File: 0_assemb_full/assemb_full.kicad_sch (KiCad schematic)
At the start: 0 parts

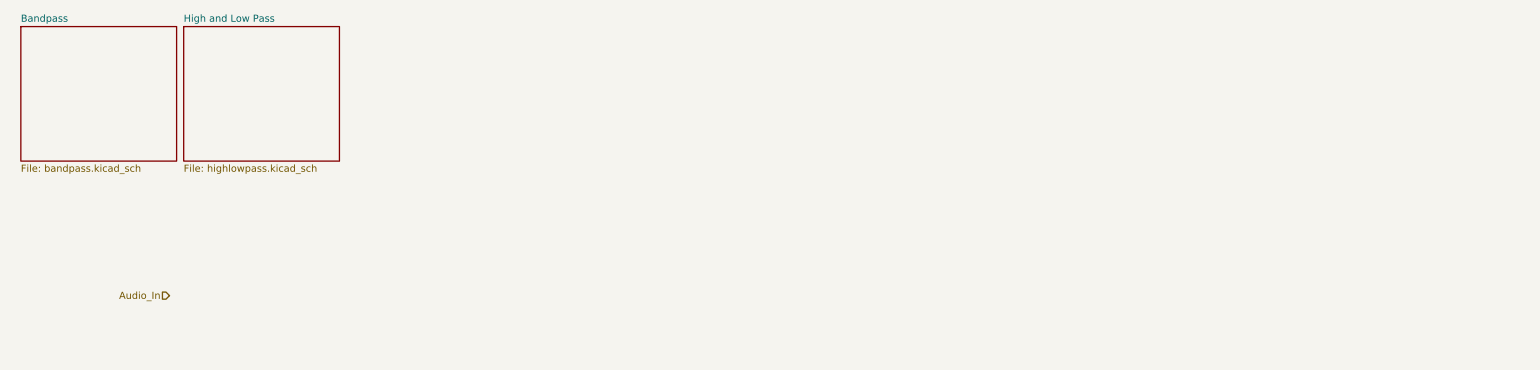
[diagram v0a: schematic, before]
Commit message: Added STM32F091RCTx symbol and power symbols
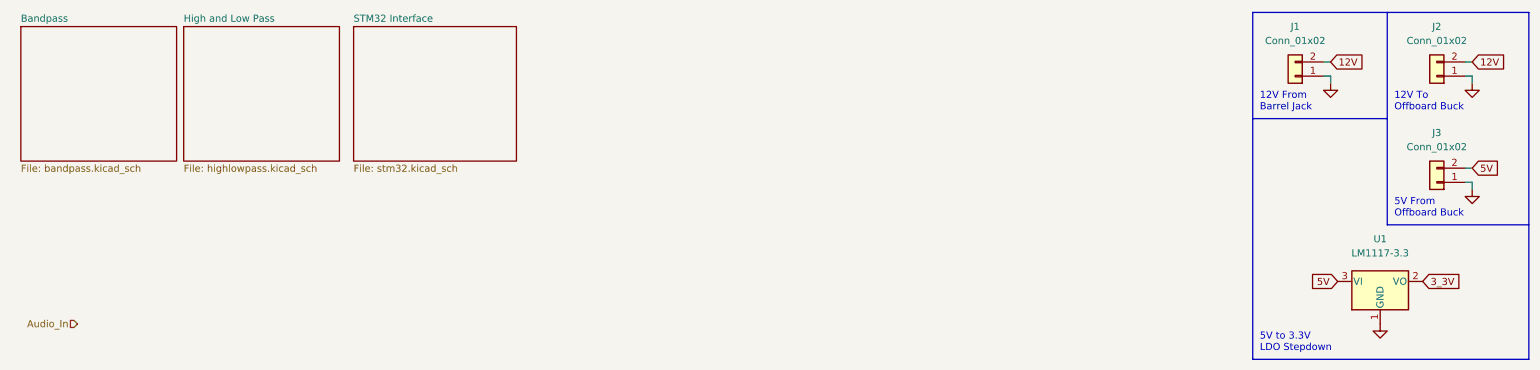
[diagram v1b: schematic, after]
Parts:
- added J1, J2, J3: Conn_01x02, symbol Connector_Generic:Conn_01x02
- added U1: LM1117-3.3, symbol Regulator_Linear:LM1117-3.3
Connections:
- new net 12V: J1.2 (Pin_2), J2.2 (Pin_2)
- new net 3_3V: U1.2 (VO)
- new net 5V: J3.2 (Pin_2), U1.3 (VI)
- new net GND: J1.1 (Pin_1), J2.1 (Pin_1), J3.1 (Pin_1), U1.1 (GND)
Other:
- added sheet STM32 Interface (stm32.kicad_sch)
- note added: "12V From Barrel Jack"
- note added: "12V To Offboard Buck"
- note added: "5V From Offboard Buck"
- note added: "5V to 3.3V LDO Stepdown"

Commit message: Additional changes
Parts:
- added C1, C2: 10u, symbol Device:C
- J1: footprint (none) -> Connector_BarrelJack:BarrelJack_CUI_PJ-102AH_Horizontal
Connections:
- net 12V: now also J1.1 (Pin_1), J2.1 (Pin_1); no longer J1.2 (Pin_2), J2.2 (Pin_2)
- net 3_3V: now also C2.1
- net 5V: now also J3.1 (Pin_1), C1.1; no longer J3.2 (Pin_2)
- net GND: now also J1.2 (Pin_2), J2.2 (Pin_2), J3.2 (Pin_2), C1.2, C2.2; no longer J1.1 (Pin_1), J2.1 (Pin_1), J3.1 (Pin_1)
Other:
- moved on the sheet: J1, J2, J3, U1

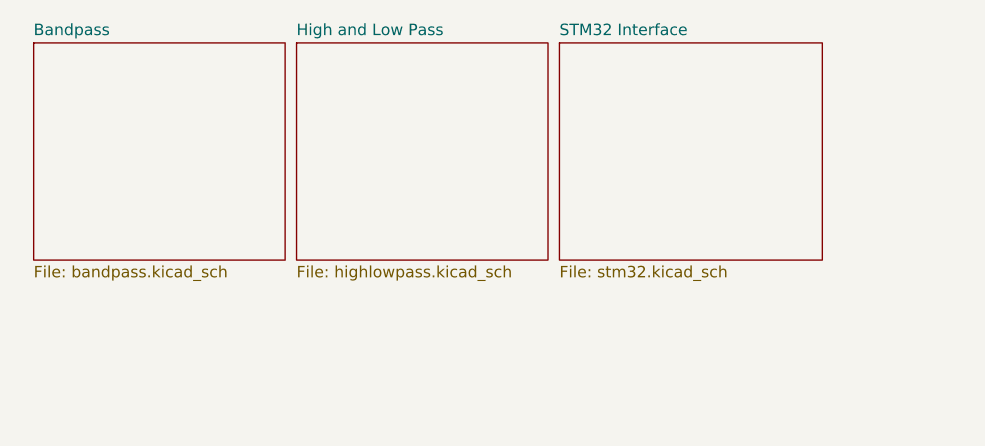
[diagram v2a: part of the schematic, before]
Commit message: Removed varistors, updated some STM32 connections
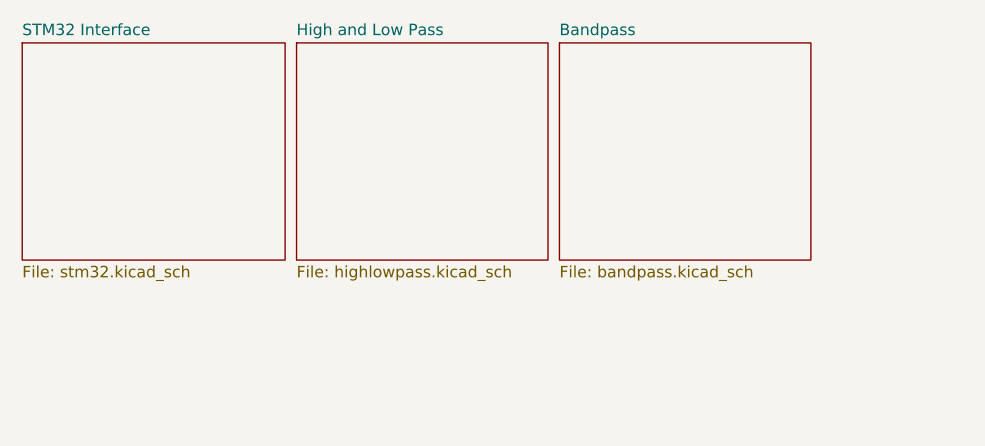
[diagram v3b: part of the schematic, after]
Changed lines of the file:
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@@
     )
   )
-  (sheet (at 13.97 15.24) (size 27.94 24.13) (fields_autoplaced)
+  (sheet (at 72.39 15.24) (size 27.94 24.13) (fields_autoplaced)
     (stroke (width 0.1524) (type solid) (color 0 0 0 0))
     (fill (color 0 0 0 0.0000))
-    (property "Sheet name" "Bandpass" (id 0) (at 13.97 14.5284 0)
+    (property "Sheet name" "Bandpass" (id 0) (at 72.39 14.5284 0)
       (effects (font (size 1.27 1.27)) (justify left bottom))
     )
-    (property "Sheet file" "bandpass.kicad_sch" (id 1) (at 13.97 39.9546 0)
+    (property "Sheet file" "bandpass.kicad_sch" (id 1) (at 72.39 39.9546 0)
       (effects (font (size 1.27 1.27)) (justify left top))
     )
   )
-  (sheet (at 72.39 15.24) (size 29.21 24.13) (fields_autoplaced)
+  (sheet (at 12.7 15.24) (size 29.21 24.13) (fields_autoplaced)
     (stroke (width 0.1524) (type solid) (color 0 0 0 0))
     (fill (color 0 0 0 0.0000))
-    (property "Sheet name" "STM32 Interface" (id 0) (at 72.39 14.5284 0)
+    (property "Sheet name" "STM32 Interface" (id 0) (at 12.7 14.5284 0)
       (effects (font (size 1.27 1.27)) (justify left bottom))
     )
-    (property "Sheet file" "stm32.kicad_sch" (id 1) (at 72.39 39.9546 0)
+    (property "Sheet file" "stm32.kicad_sch" (id 1) (at 12.7 39.9546 0)
       (effects (font (size 1.27 1.27)) (justify left top))
     )
@@
       (reference "J4") (unit 1) (value "Conn_01x02") (footprint "")
     )
+    (path "/4d0bd211-4794-4141-8b4c-fc5ed36fe38a/100fdcba-4ad6-4620-94f4-7ddc5776d3cc"
+      (reference "J5") (unit 1) (value "SPIConn_01x03") (footprint "")
+    )
     (path "/27872fd8-6da5-4d41-bede-b1346c5a5ef3/3c1be632-0e4c-4cdc-9b28-367769451b36"
-      (reference "R1") (unit 1) (value "470") (footprint "")
+      (reference "R1") (unit 1) (value "220") (footprint "")
     )
     (path "/27872fd8-6da5-4d41-bede-b1346c5a5ef3/9db6d9c8-1e04-4846-be6b-7548dbb58116"
-      (reference "R2") (unit 1) (value "470") (footprint "")
+      (reference "R2") (unit 1) (value "220") (footprint "")
     )
     (path "/27872fd8-6da5-4d41-bede-b1346c5a5ef3/83a6c34b-cd42-4bc3-8098-00e2f2514636"
@@
     )
     (path "/27872fd8-6da5-4d41-bede-b1346c5a5ef3/710dc276-e229-4000-a5ad-052650e37413"
-      (reference "R5") (unit 1) (value "470") (footprint "")
+      (reference "R5") (unit 1) (value "220") (footprint "")
     )
     (path "/27872fd8-6da5-4d41-bede-b1346c5a5ef3/05c4cbb0-a462-4ca4-b4c1-4ab919f030b3"
@@
     )
     (path "/016209f3-6b0c-4be6-bf7f-4e52cc050e04/6322e136-6565-4534-9cec-e553b466d6c3"
-      (reference "R26") (unit 1) (value "470") (footprint "")
+      (reference "R26") (unit 1) (value "220") (footprint "")
     )
     (path "/016209f3-6b0c-4be6-bf7f-4e52cc050e04/1fd93811-7681-45f0-be35-117fd0697e16"
-      (reference "R27") (unit 1) (value "4.7K") (footprint "")
+      (reference "R27") (unit 1) (value "680") (footprint "")
     )
     (path "/016209f3-6b0c-4be6-bf7f-4e52cc050e04/1adaa2cb-5868-4644-a777-0e0cd70303f5"
@@
     )
     (path "/016209f3-6b0c-4be6-bf7f-4e52cc050e04/838c7b61-f247-4811-b006-4589bd547892"
-      (reference "R42") (unit 1) (value "470") (footprint "")
+      (reference "R42") (unit 1) (value "220") (footprint "")
     )
     (path "/016209f3-6b0c-4be6-bf7f-4e52cc050e04/e6682f13-8da5-4feb-96ee-693438046242"
@@
     )
     (path "/016209f3-6b0c-4be6-bf7f-4e52cc050e04/8175f77f-1f13-4606-801a-a25d1b77be96"
-      (reference "R45") (unit 1) (value "330") (footprint "")
+      (reference "R45") (unit 1) (value "150") (footprint "")
     )
     (path "/016209f3-6b0c-4be6-bf7f-4e52cc050e04/5ff1d421-f058-4c00-a35d-653f9896f96f"
@@
       (reference "R58") (unit 1) (value "100K") (footprint "")
     )
-    (path "/27872fd8-6da5-4d41-bede-b1346c5a5ef3/86de8196-9bb4-4958-9d15-f4b9c104935b"
-      (reference "RV1") (unit 1) (value "1K") (footprint "")
-    )
-    (path "/27872fd8-6da5-4d41-bede-b1346c5a5ef3/d817147e-f3d1-4948-a7ac-9bc6cf3a8b08"
-      (reference "RV2") (unit 1) (value "1K") (footprint "")
-    )
-    (path "/27872fd8-6da5-4d41-bede-b1346c5a5ef3/1bcd90d8-ea3a-45ad-93f3-8f1c8cea09d3"
-      (reference "RV3") (unit 1) (value "1K") (footprint "")
-    )
-    (path "/016209f3-6b0c-4be6-bf7f-4e52cc050e04/20368424-e0c8-4202-a8a7-d2a77028b7d5"
-      (reference "RV4") (unit 1) (value "1K") (footprint "")
-    )
-    (path "/016209f3-6b0c-4be6-bf7f-4e52cc050e04/b85f2704-e5e8-42e4-b2b2-4e2c7e2225dd"
-      (reference "RV5") (unit 1) (value "10K") (footprint "")
-    )
-    (path "/016209f3-6b0c-4be6-bf7f-4e52cc050e04/ac26d519-1e26-4e03-8b77-68d694fbb77f"
-      (reference "RV6") (unit 1) (value "1K") (footprint "")
-    )
-    (path "/016209f3-6b0c-4be6-bf7f-4e52cc050e04/f9b2ebb7-9757-4a5b-8dcc-2c57fc590e02"
-      (reference "RV7") (unit 1) (value "680") (footprint "")
-    )
     (path "/d3e0143d-69a2-4508-8939-8f6315ecceac"

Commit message: A bunch of changes to the schematics
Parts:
- removed J2, J3: Conn_01x02, symbol Connector_Generic:Conn_01x02
- added J?: Conn_02x06, symbol Connector_Generic:Conn_02x06_Counter_Clockwise
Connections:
- net 12V: now also J?.4 (Pin_4), J?.9 (Pin_9)
- net 5V: now also J?.1 (Pin_1), J?.12 (Pin_12)
- net GND: now also J?.10 (Pin_10), J?.11 (Pin_11), J?.2 (Pin_2), J?.3 (Pin_3)
- new net 12VRP: J?.5 (Pin_5), J?.8 (Pin_8)
- new net ENB: J?.6 (Pin_6)
- new net PGB: J?.7 (Pin_7)
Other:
- note added: "Buck Connections"
- note added: "Copy from STM32 Dev Board?"
- note removed: "12V To Offboard Buck"
- note removed: "5V From Offboard Buck"
- moved on the sheet: C1, C2, U1

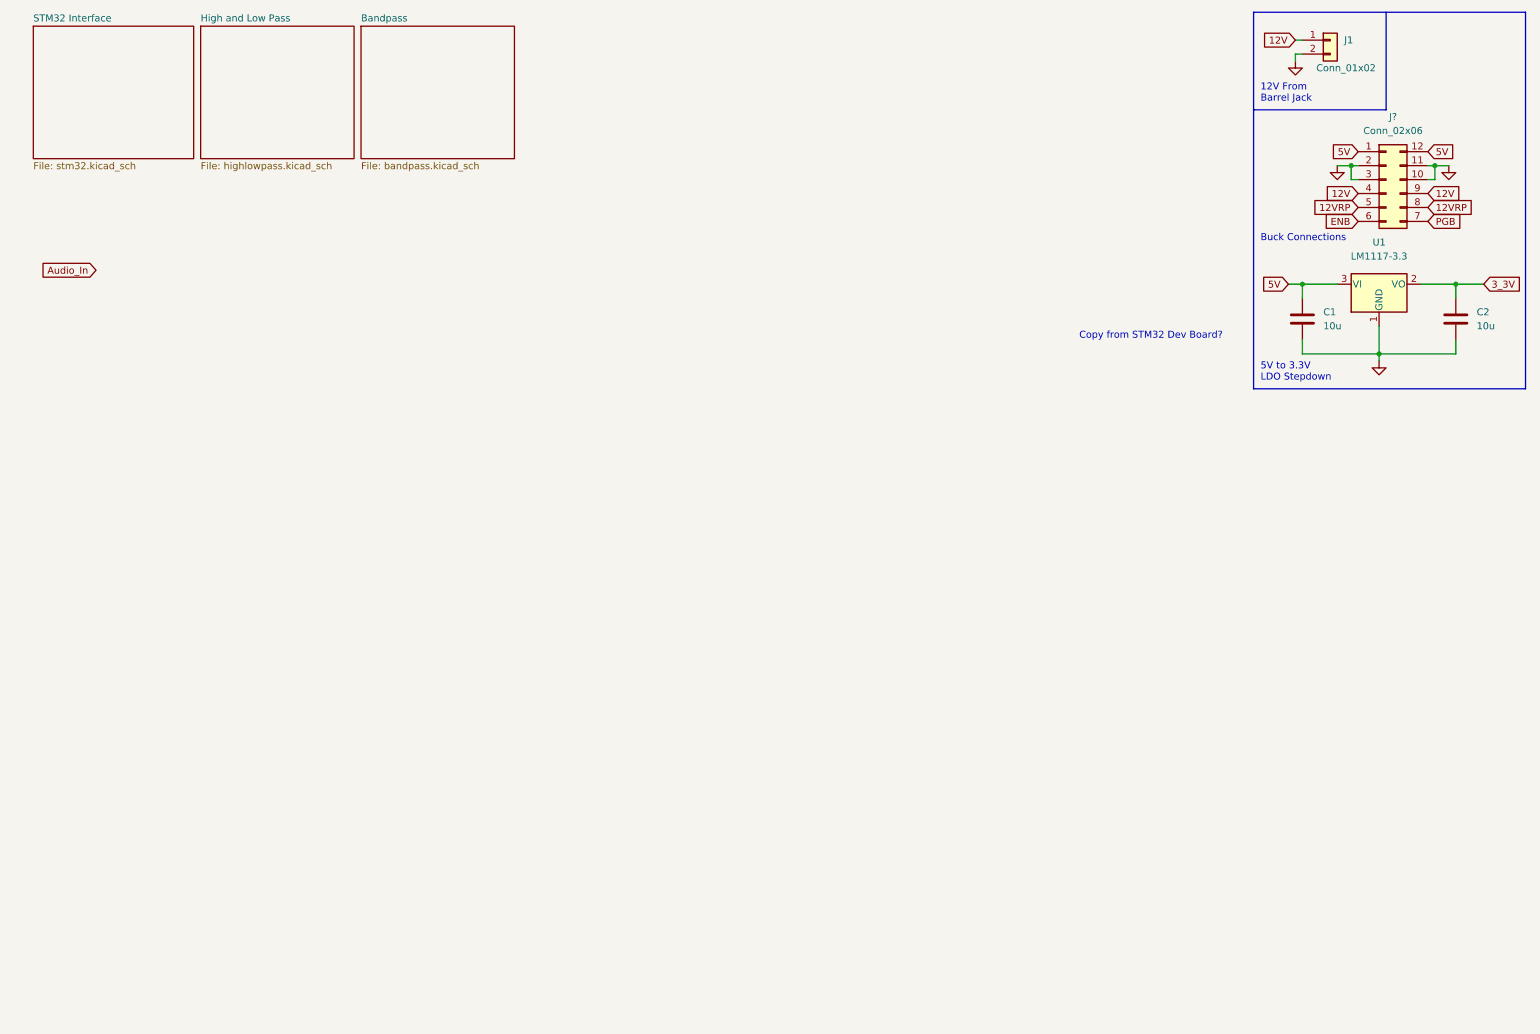
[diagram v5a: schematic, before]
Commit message: Updates to the filter system
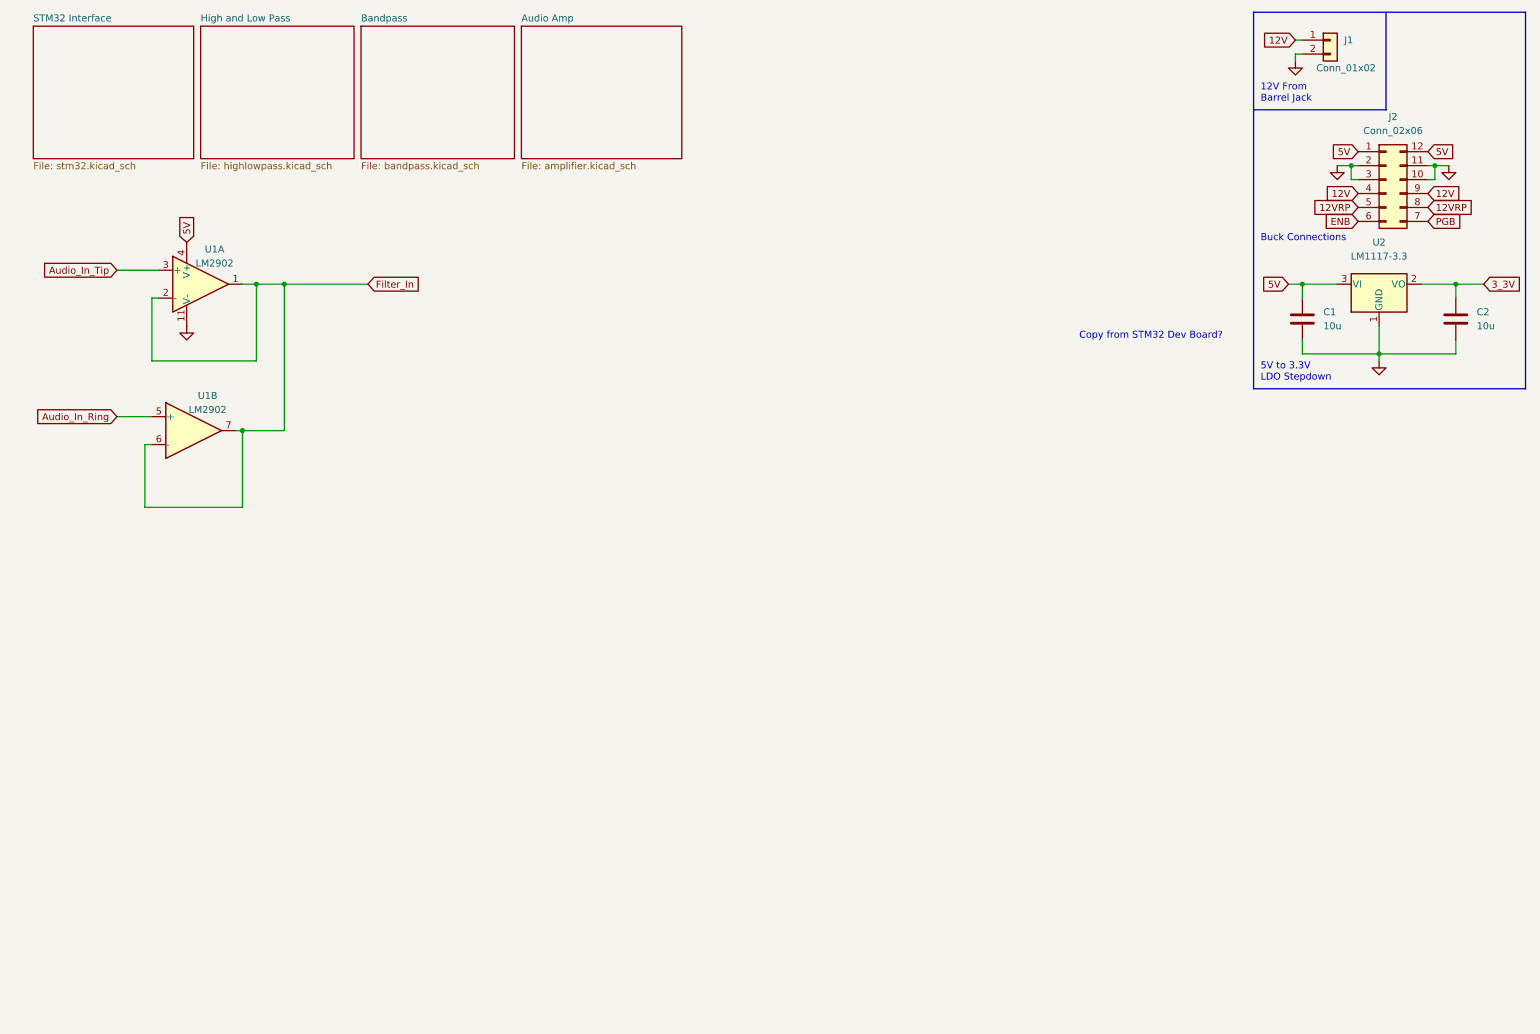
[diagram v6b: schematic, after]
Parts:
- added U1: LM2902, symbol Amplifier_Operational:LM2902
- gave numbers to parts that had none: 1
- renumbered U1 to U2
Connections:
- net 5V: now also U1.4 (V+)
- net GND: now also U1.11 (V-)
- new net Audio_In_Ring: U1.5 (+)
- new net Audio_In_Tip: U1.3 (+)
- new net Filter_In: U1.1, U1.2 (-), U1.6 (-), U1.7
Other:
- added sheet Audio Amp (amplifier.kicad_sch)

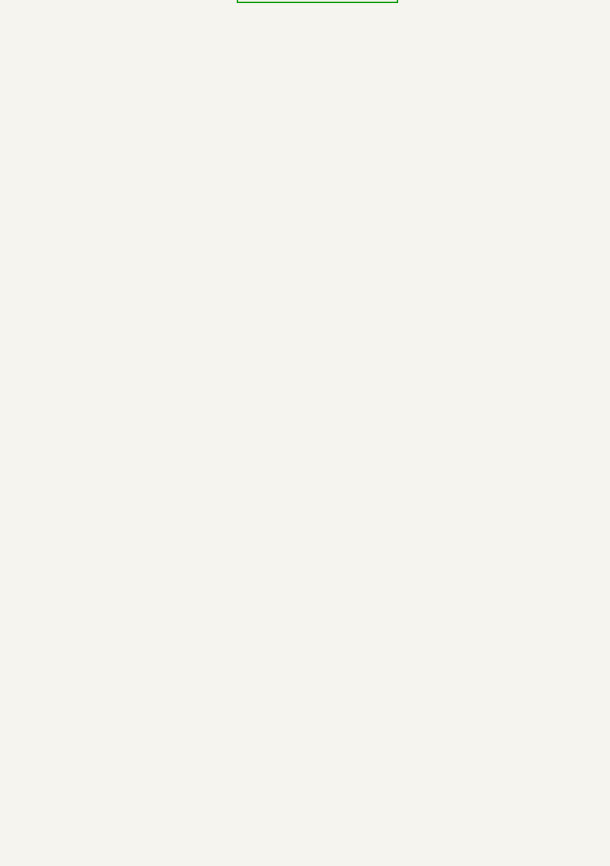
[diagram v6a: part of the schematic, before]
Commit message: Added amplifier circuit and the programming header.
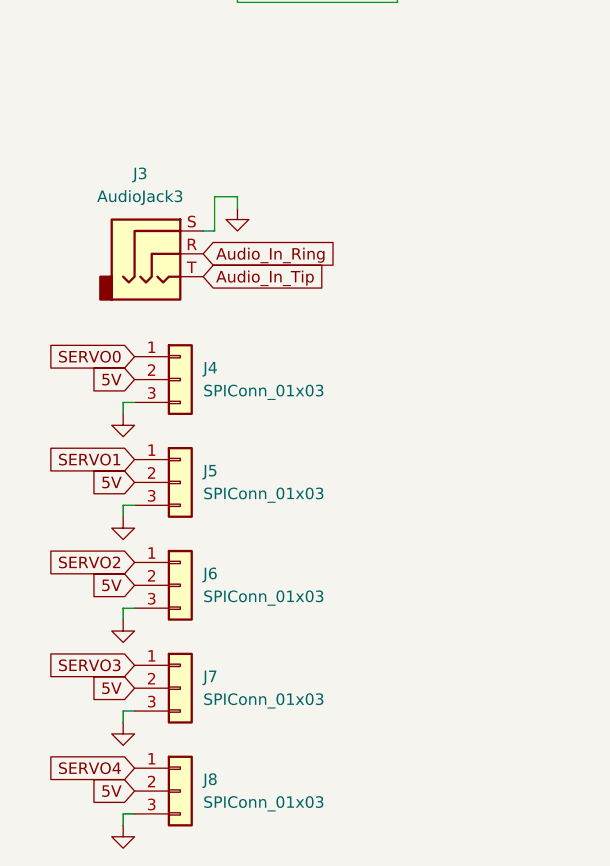
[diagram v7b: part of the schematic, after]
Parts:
- added J3: AudioJack3, symbol Connector:AudioJack3
- added J4, J5, J6, J7, J8: SPIConn_01x03, symbol Connector_Generic:Conn_01x03
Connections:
- net 5V: now also J4.2 (Pin_2), J5.2 (Pin_2), J6.2 (Pin_2), J7.2 (Pin_2), J8.2 (Pin_2)
- net Audio_In_Ring: now also J3.R
- net Audio_In_Tip: now also J3.T
- net GND: now also J3.S, J4.3 (Pin_3), J5.3 (Pin_3), J6.3 (Pin_3), J7.3 (Pin_3), J8.3 (Pin_3)
- new net SERVO0: J4.1 (Pin_1)
- new net SERVO1: J5.1 (Pin_1)
- new net SERVO2: J6.1 (Pin_1)
- new net SERVO3: J7.1 (Pin_1)
- new net SERVO4: J8.1 (Pin_1)
